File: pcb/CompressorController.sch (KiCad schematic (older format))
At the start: 13 parts

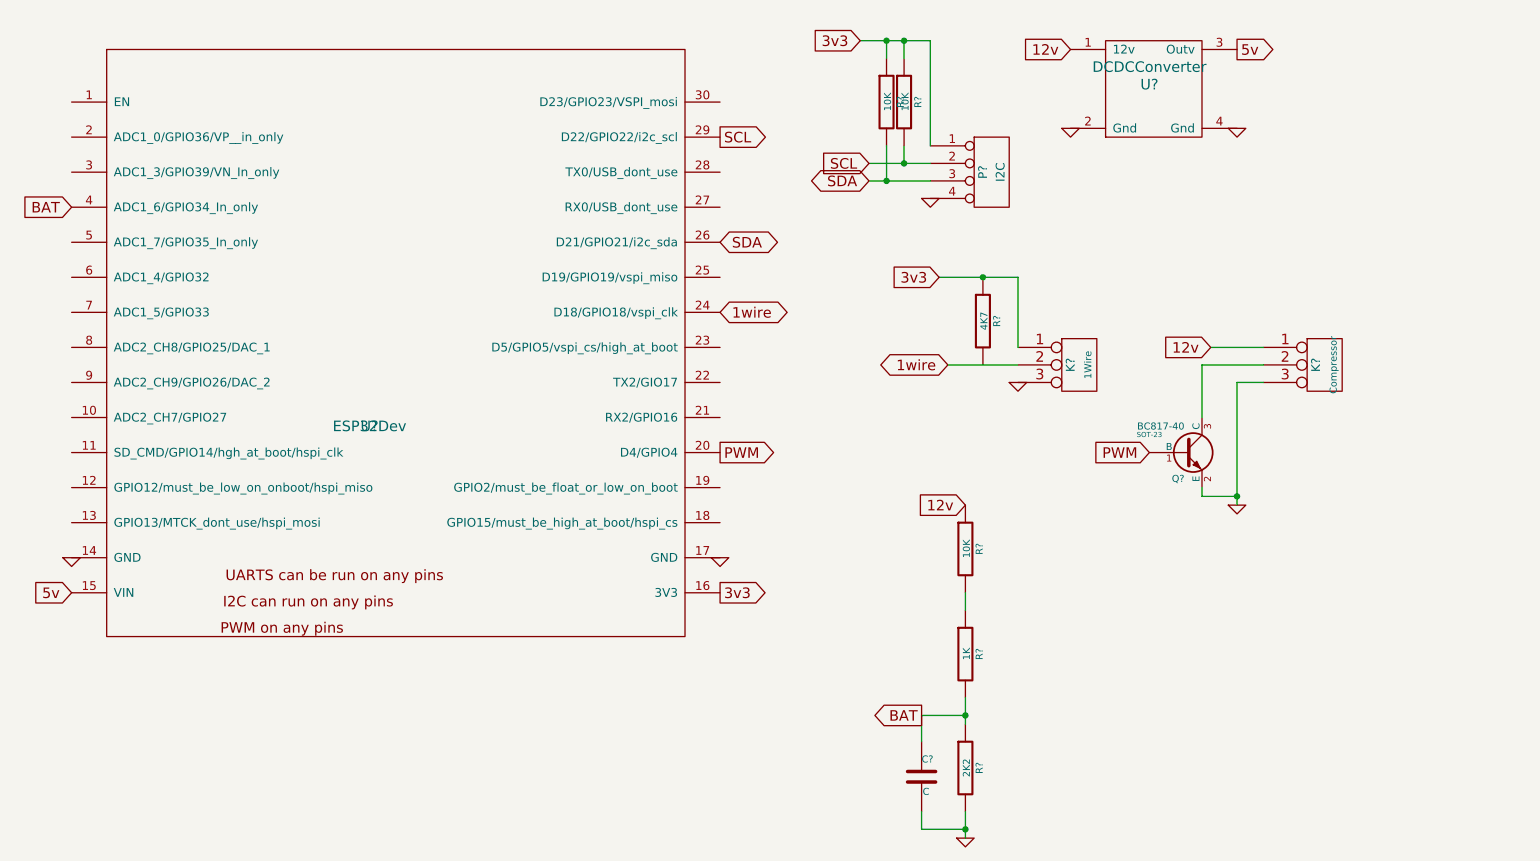
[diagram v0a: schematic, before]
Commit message: Added display
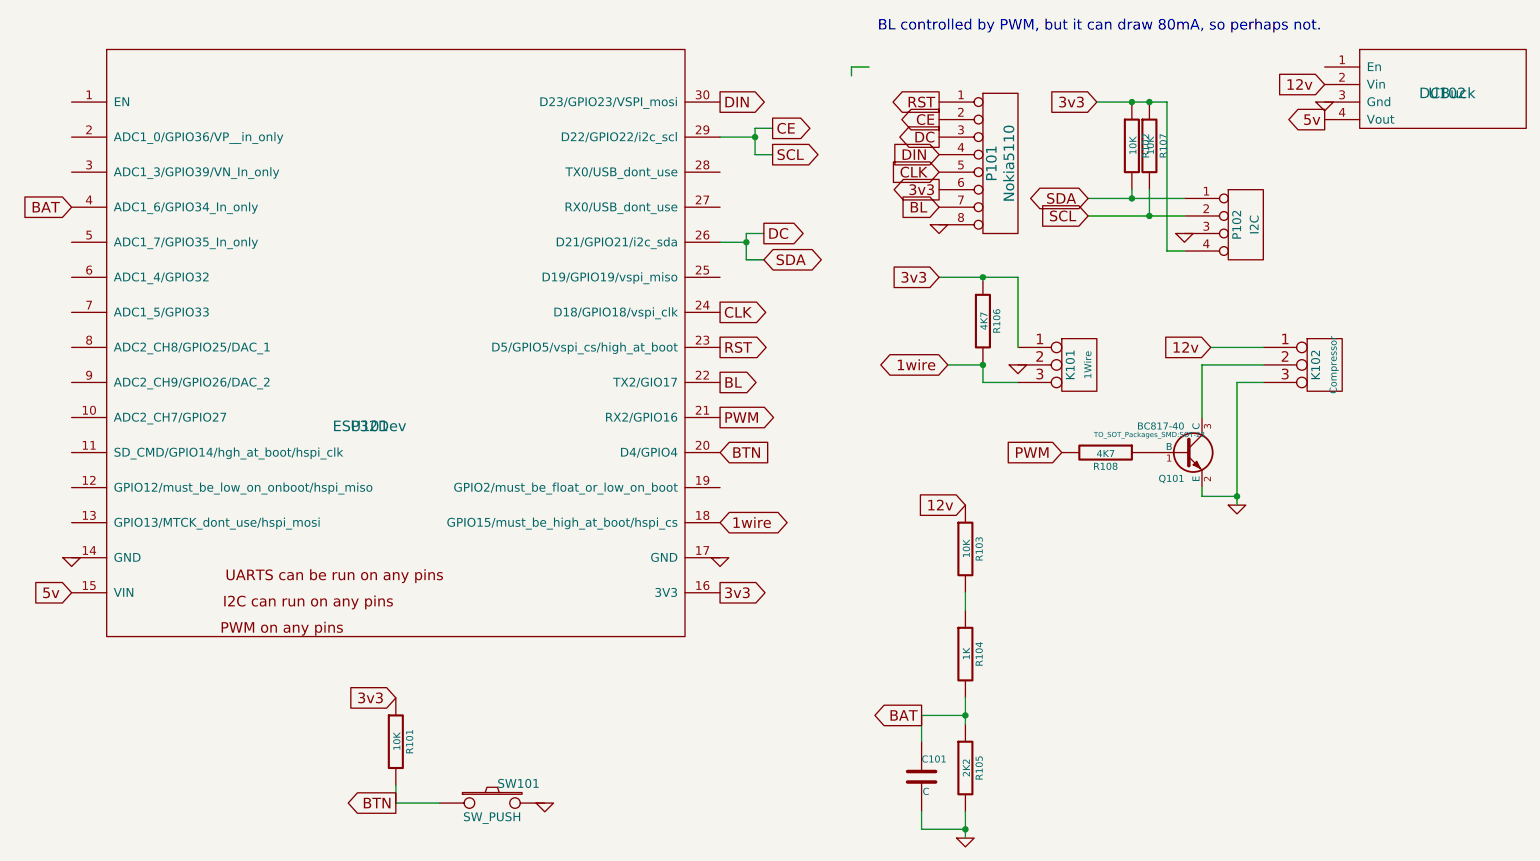
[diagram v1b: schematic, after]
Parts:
- removed P?: I2C, symbol CONN_4
- removed R? (x2): 10K, symbol R
- removed U?: DCDCConverter, symbol DCDCConverter
- added P101: Nokia5110, Pin_Headers:Pin_Header_Straight_1x08, symbol CONN_8
- added P102: I2C, Pin_Headers:Pin_Header_Straight_1x04, symbol CONN_4
- added R101, R102, R107: 10K, Resistors_SMD:R_0805_HandSoldering, symbol R
- added R108: 4K7, Resistors_SMD:R_0805_HandSoldering, symbol R
- added SW101: SW_PUSH, Buttons_Switches_ThroughHole:SW_PUSH_6mm, symbol SW_PUSH
- added U102: DCBuck, Divers:DCBuckModule, symbol DCBuck
- C101: renamed from C?; footprint (none) -> Capacitors_SMD:C_0805_HandSoldering
- K101, K102: renamed from K?; footprint (none) -> Connect:bornier3
- Q101: renamed from Q?; footprint SOT-23 -> TO_SOT_Packages_SMD:SOT-23
- R103, R104, R105, R106: renamed from R?; footprint (none) -> Resistors_SMD:R_0805_HandSoldering
- U101: renamed from U?; footprint (none) -> Divers:ESP32Dev
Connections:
- net labels added: BL, BTN, CE, CLK, DC, DIN, RST
- wire segments 25 -> 38
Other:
- note added: "BL controlled by PWM, but it can draw 80mA, so perhaps not.\n\n"
